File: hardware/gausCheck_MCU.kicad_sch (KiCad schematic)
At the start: 1 part, among them U3 ATSAML22N18A-AUT

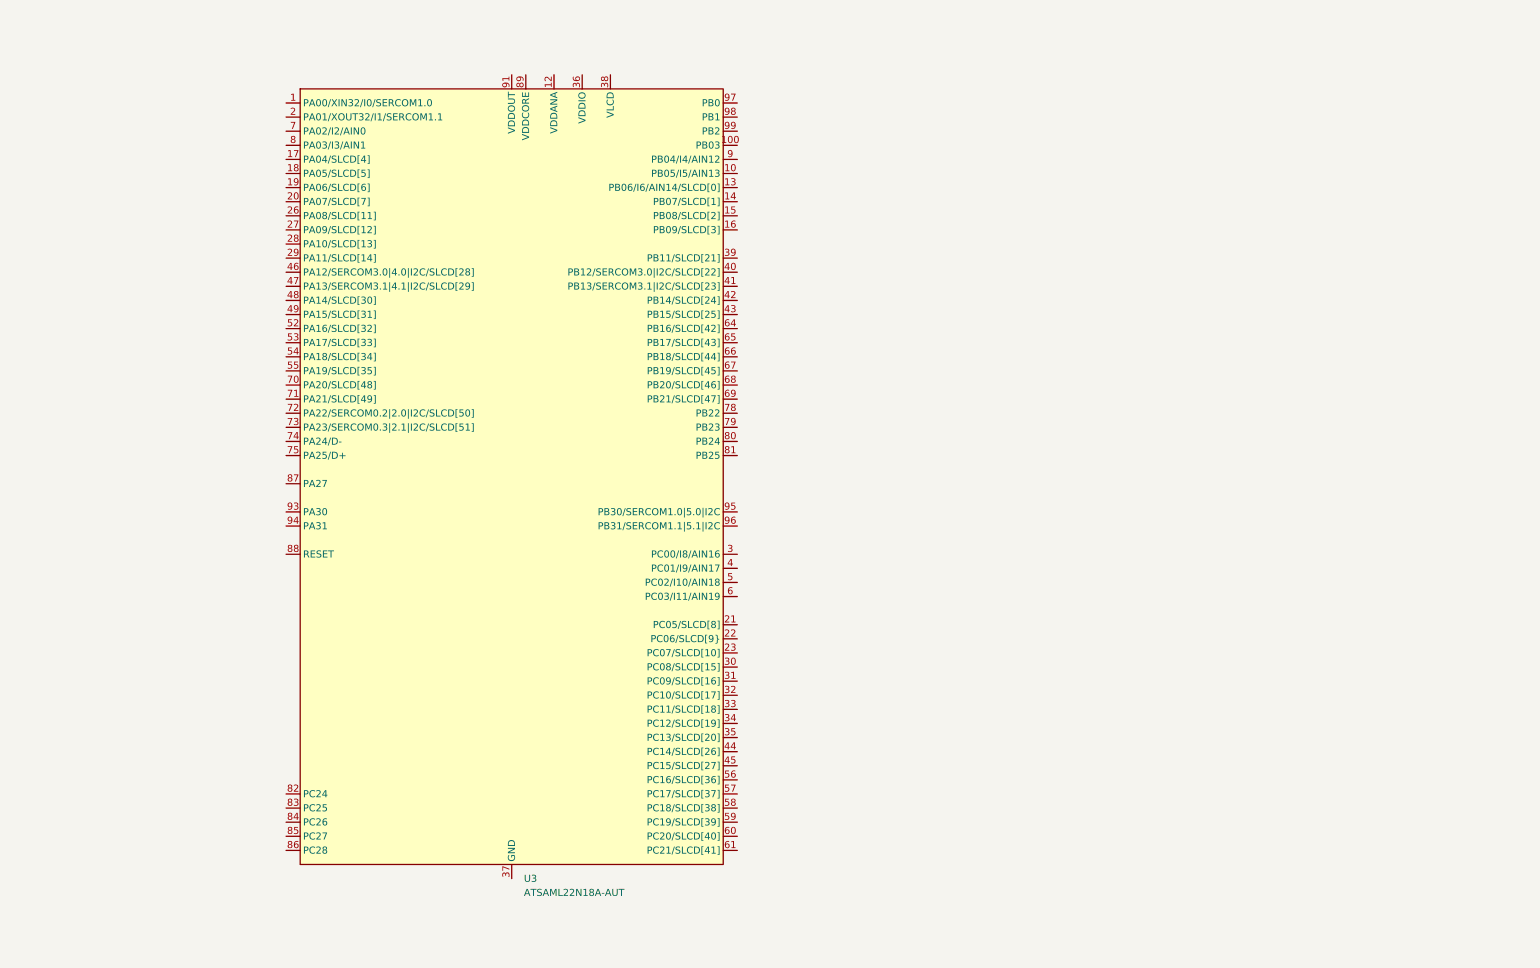
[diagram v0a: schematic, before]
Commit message: SCH - display lines
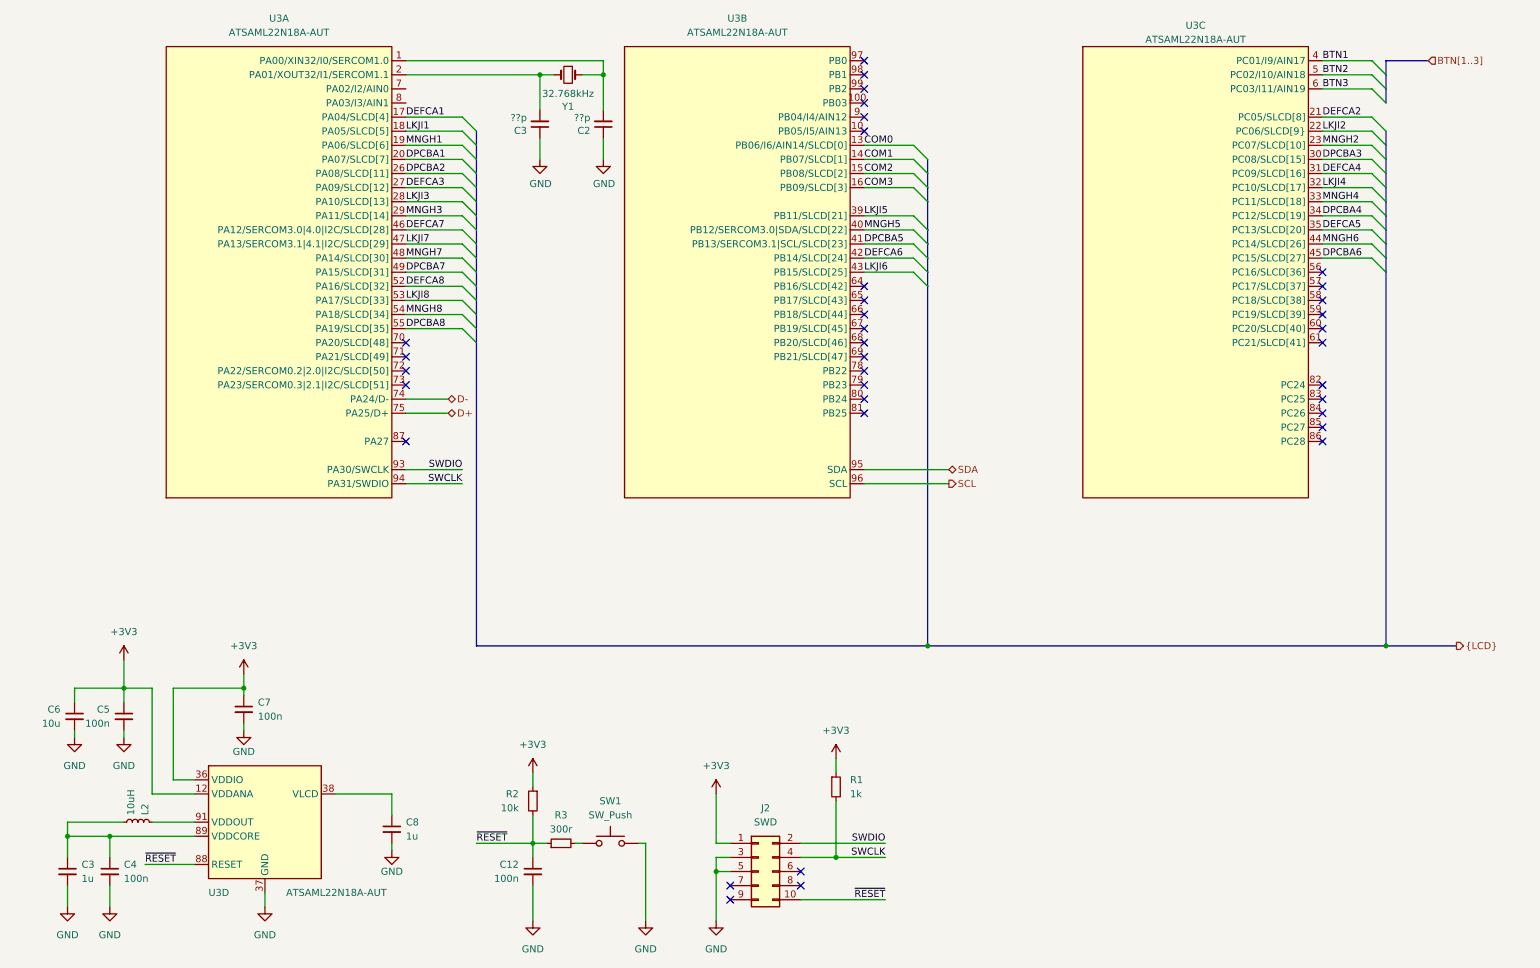
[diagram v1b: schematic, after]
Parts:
- removed U3: ATSAML22N18A-AUT, Package_QFP:TQFP-100_14x14mm_P0.5mm, symbol GaussCheckCustomSymbols:ATSAML22N18A-AUT
- added C12, C4, C5, C7: 100n, symbol Device:C_Small
- added C2, C3: ??p, Capacitor_SMD:C_0603_1608Metric, symbol MagnetoStage-rescue:C_Small-Device
- added C3, C8: 1u, symbol Device:C_Small
- added C6: 10u, symbol Device:C_Small
- added J2: SWD, symbol Connector_Generic:Conn_02x05_Odd_Even
- added L2: 10uH, symbol Device:L_Small
- added R1: 1k, symbol Device:R_Small
- added R2: 10k, symbol Device:R_Small
- added R3: 300r, symbol Device:R_Small
- added SW1: SW_Push, symbol Switch:SW_Push
- added U3: ATSAML22N18A-AUT, Package_QFP:TQFP-100_14x14mm_P0.5mm, symbol GaussCheckCustomSymbols:ATSAML22N18A-AUT (Multi)
- added Y1: 32.768kHz, Crystal:Crystal_SMD_3215-2Pin_3.2x1.5mm, symbol MagnetoStage-rescue:Crystal_32.7680kHz_12.5pF_SMD-Knochi_Crystals
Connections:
- new net: R3.2, SW1.1
- new net: C3.1, C4.1, L2.2, U3.89 (VDDCORE)
- new net: L2.1, U3.91 (VDDOUT)
- new net: C8.1, U3.38 (VLCD)
- new net: C2.2, U3.1 (PA00/XIN32/I0/SERCOM1.0), Y1.1
- new net: C3.2, U3.2 (PA01/XOUT32/I1/SERCOM1.1), Y1.4
- new net +3V3: C5.1, C6.1, C7.1, J2.1 (Pin_1), R1.1, R2.1, U3.12 (VDDANA), U3.25 (VDDANA), U3.36 (VDDIO), U3.51 (VDDIO), U3.63 (VDDIO), U3.77 (VDDIO), U3.92 (VDDIO)
- new net BTN1: U3.4 (PC01/I9/AIN17)
- new net BTN2: U3.5 (PC02/I10/AIN18)
- new net BTN3: U3.6 (PC03/I11/AIN19)
- new net COM0: U3.13 (PB06/I6/AIN14/SLCD[0])
- new net COM1: U3.14 (PB07/SLCD[1])
- new net COM2: U3.15 (PB08/SLCD[2])
- new net COM3: U3.16 (PB09/SLCD[3])
- new net D+: U3.75 (PA25/D+)
- new net D-: U3.74 (PA24/D-)
- new net DEFCA1: U3.17 (PA04/SLCD[4])
- new net DEFCA2: U3.21 (PC05/SLCD[8])
- new net DEFCA3: U3.27 (PA09/SLCD[12])
- new net DEFCA4: U3.31 (PC09/SLCD[16])
- new net DEFCA5: U3.35 (PC13/SLCD[20])
- new net DEFCA6: U3.42 (PB14/SLCD[24])
- new net DEFCA7: U3.46 (PA12/SERCOM3.0|4.0|I2C/SLCD[28])
- new net DEFCA8: U3.52 (PA16/SLCD[32])
- new net DPCBA1: U3.20 (PA07/SLCD[7])
- new net DPCBA2: U3.26 (PA08/SLCD[11])
- new net DPCBA3: U3.30 (PC08/SLCD[15])
- new net DPCBA4: U3.34 (PC12/SLCD[19])
- new net DPCBA5: U3.41 (PB13/SERCOM3.1|SCL/SLCD[23])
- new net DPCBA6: U3.45 (PC15/SLCD[27])
- new net DPCBA7: U3.49 (PA15/SLCD[31])
- new net DPCBA8: U3.55 (PA19/SLCD[35])
- new net GND: C12.2, C2.1, C3.1, C3.2, C4.2, C5.2, C6.2, C7.2, C8.2, J2.3 (Pin_3), J2.5 (Pin_5), SW1.2, U3.11 (GND), U3.24 (GND), U3.37 (GND), U3.50 (GND), U3.62 (GND), U3.76 (GND), U3.90 (GND)
- new net LKJI1: U3.18 (PA05/SLCD[5])
- new net LKJI2: U3.22 (PC06/SLCD[9})
- new net LKJI3: U3.28 (PA10/SLCD[13])
- new net LKJI4: U3.32 (PC10/SLCD[17])
- new net LKJI5: U3.39 (PB11/SLCD[21])
- new net LKJI6: U3.43 (PB15/SLCD[25])
- new net LKJI7: U3.47 (PA13/SERCOM3.1|4.1|I2C/SLCD[29])
- new net LKJI8: U3.53 (PA17/SLCD[33])
- new net MNGH1: U3.19 (PA06/SLCD[6])
- new net MNGH2: U3.23 (PC07/SLCD[10])
- new net MNGH3: U3.29 (PA11/SLCD[14])
- new net MNGH4: U3.33 (PC11/SLCD[18])
- new net MNGH5: U3.40 (PB12/SERCOM3.0|SDA/SLCD[22])
- new net MNGH6: U3.44 (PC14/SLCD[26])
- new net MNGH7: U3.48 (PA14/SLCD[30])
- new net MNGH8: U3.54 (PA18/SLCD[34])
- new net SCL: U3.96 (PB31/SERCOM1.1|5.1|SCL)
- new net SDA: U3.95 (PB30/SERCOM1.0|5.0|SDA)
- new net SWCLK: J2.4 (Pin_4), R1.2, U3.94 (PA31/SWDIO)
- new net SWDIO: J2.2 (Pin_2), U3.93 (PA30/SWCLK)
- new net ~{RESET}: C12.1, J2.10 (Pin_10), R2.2, R3.1, U3.88 (RESET)
- no-connect marks 0 -> 36

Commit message: more schematic work, added buttons and led lcd wiring done
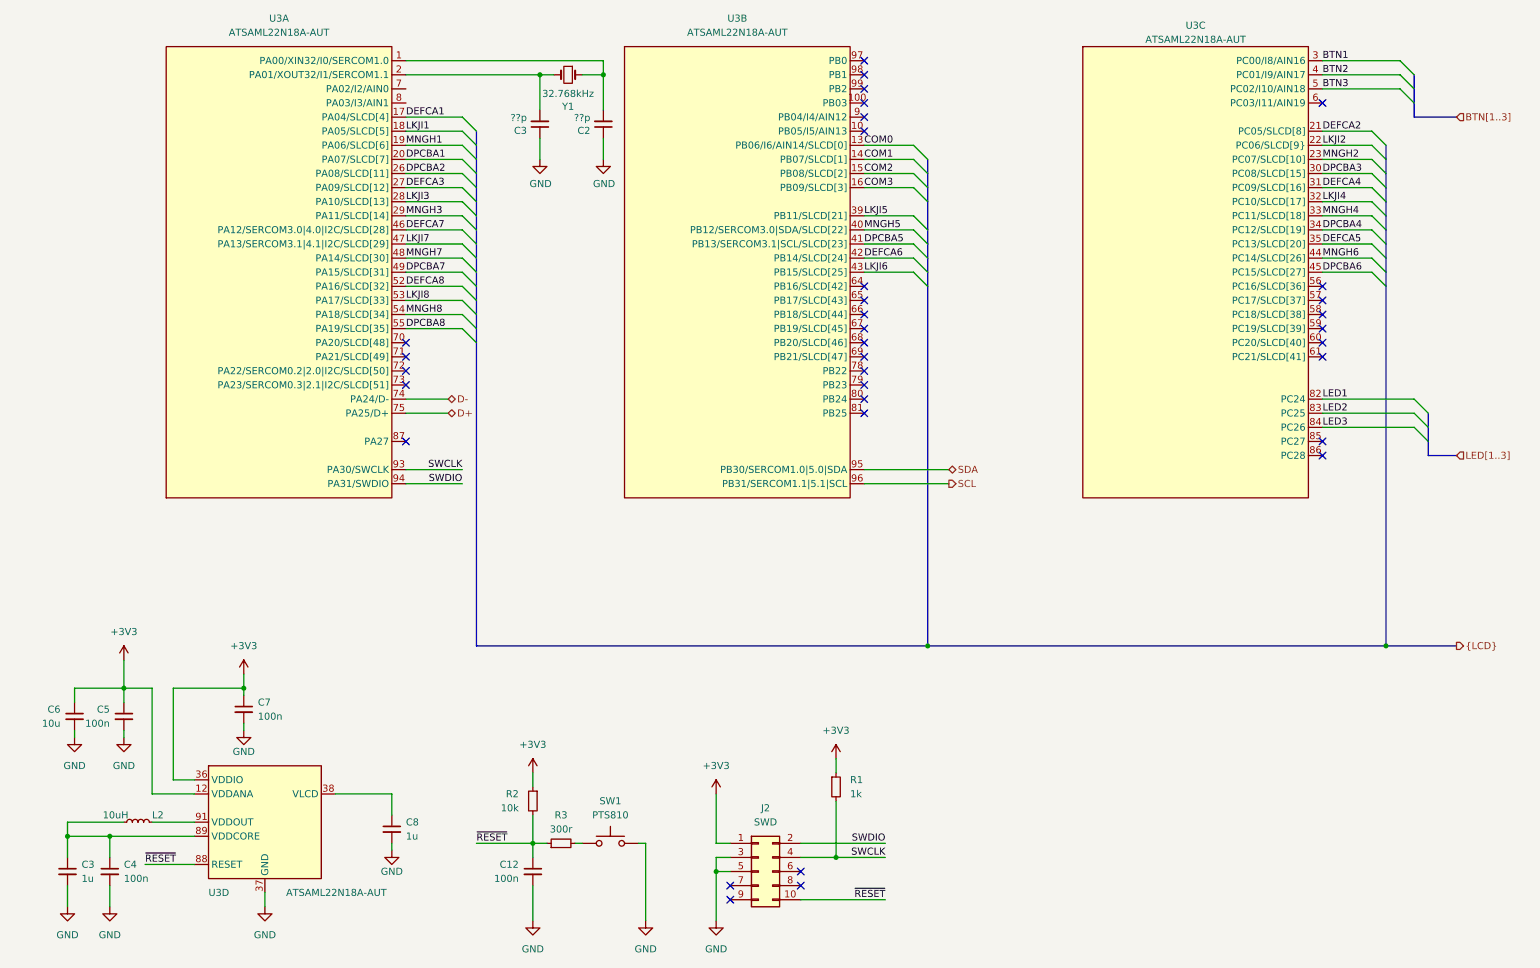
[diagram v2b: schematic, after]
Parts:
- C12, C3, C4, C5, C6, C7, C8: footprint (none) -> Capacitor_SMD:C_0603_1608Metric
- J2: footprint (none) -> Connector_PinHeader_1.27mm:PinHeader_2x05_P1.27mm_Vertical_SMD
- L2: footprint (none) -> Inductor_SMD:L_Taiyo-Yuden_MD-4040; MPN (none) -> LSXBD4040KKL100M
- R1, R2, R3: footprint (none) -> Resistor_SMD:R_0603_1608Metric
- SW1: value SW_Push -> PTS810; footprint (none) -> Button_Switch_SMD:SW_SPST_PTS810
- Y1: symbol MagnetoStage-rescue:Crystal_32.7680kHz_12.5pF_SMD-Knochi_Crystals -> Device:Crystal_Small
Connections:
- net BTN1: now also U3.3 (PC00/I8/AIN16); no longer U3.4 (PC01/I9/AIN17)
- net BTN2: now also U3.4 (PC01/I9/AIN17); no longer U3.5 (PC02/I10/AIN18)
- net BTN3: now also U3.5 (PC02/I10/AIN18); no longer U3.6 (PC03/I11/AIN19)
- net SWCLK: now also U3.93 (PA30/SWCLK); no longer U3.94 (PA31/SWDIO)
- net SWDIO: now also U3.94 (PA31/SWDIO); no longer U3.93 (PA30/SWCLK)
- net at C3.2, U3.2 (PA01/XOUT32/I1/SERCOM1.1): now also Y1.2; no longer Y1.4
- net LED1: now reaches U3.82 (PC24)
- net LED2: now reaches U3.83 (PC25)
- net LED3: now reaches U3.84 (PC26)
- no-connect marks 36 -> 34

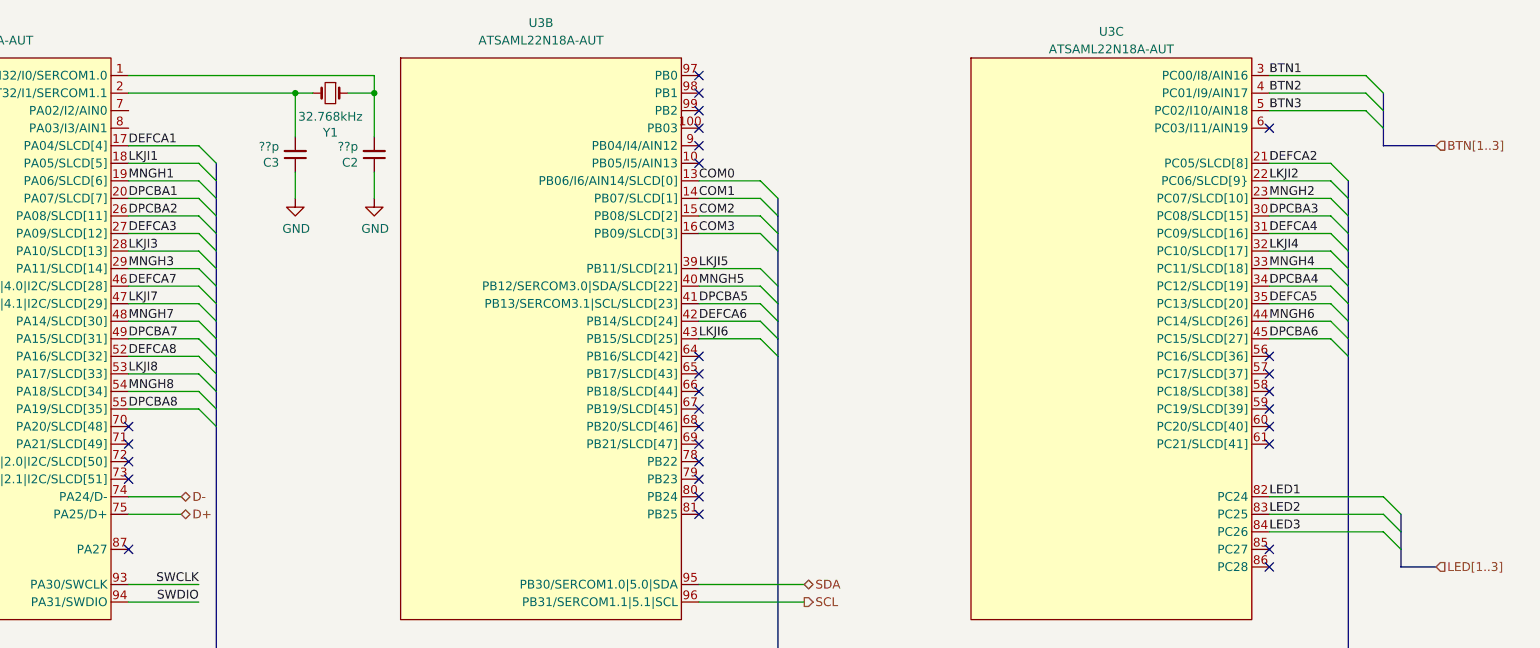
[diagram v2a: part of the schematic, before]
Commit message: change btn in sch, routing
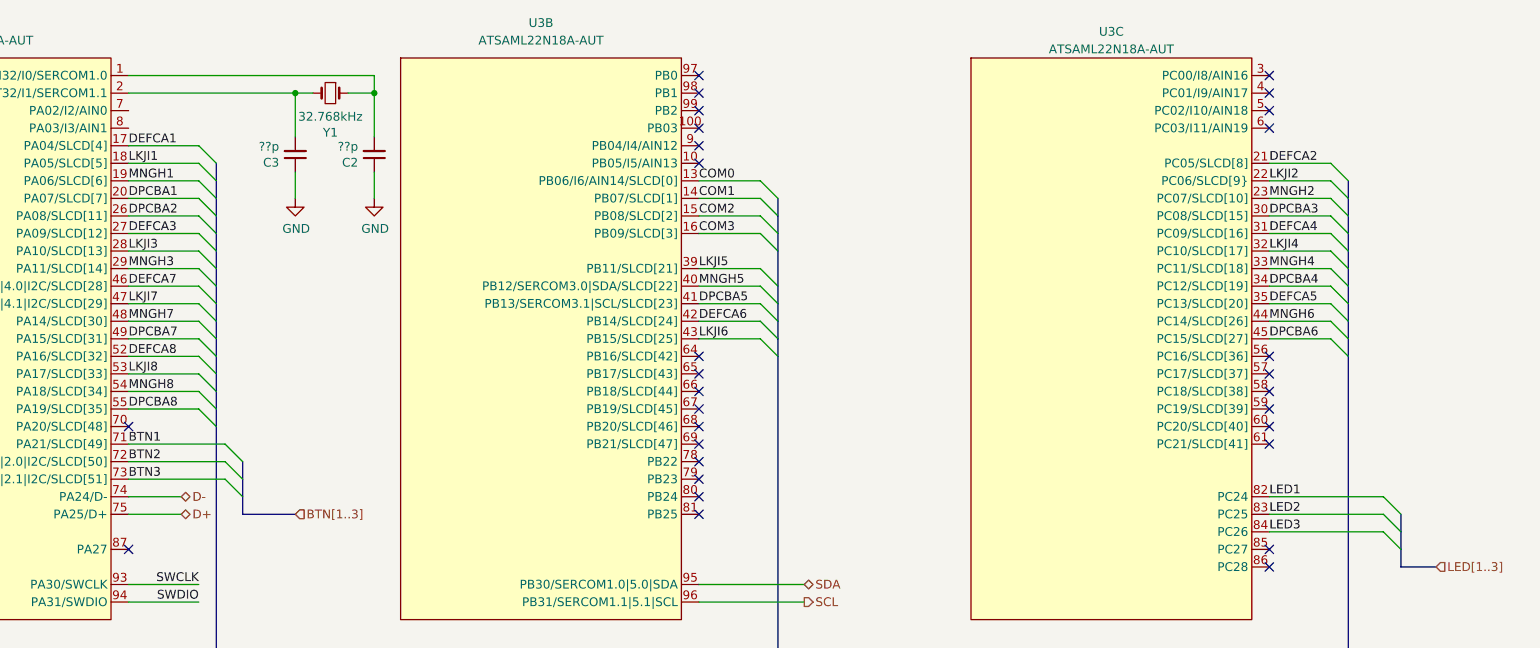
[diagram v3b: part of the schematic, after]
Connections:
- net BTN1: now also U3.71 (PA21/SLCD[49]); no longer U3.3 (PC00/I8/AIN16)
- net BTN2: now also U3.72 (PA22/SERCOM0.2|2.0|I2C/SLCD[50]); no longer U3.4 (PC01/I9/AIN17)
- net BTN3: now also U3.73 (PA23/SERCOM0.3|2.1|I2C/SLCD[51]); no longer U3.5 (PC02/I10/AIN18)

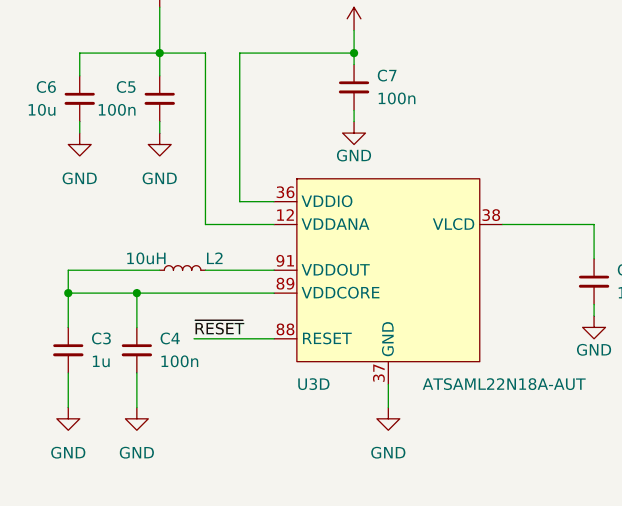
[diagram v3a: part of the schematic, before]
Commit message: Turned MCU by 45degress and rerouted
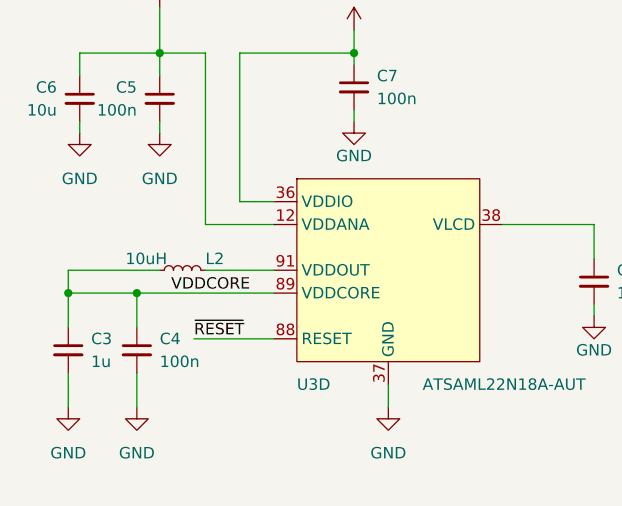
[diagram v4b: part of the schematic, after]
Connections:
- net VDDCORE: now reaches C3.1, C4.1, L2.2, U3.89 (VDDCORE)
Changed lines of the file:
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@@
+    (effects (font (size 1.27 1.27)) (justify left bottom))
+  )
+  (label "VDDCORE" (at 33.02 170.18 0) (fields_autoplaced)
     (effects (font (size 1.27 1.27)) (justify left bottom))
   )

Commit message: minor adjustments
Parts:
- L2: footprint Inductor_SMD:L_Taiyo-Yuden_MD-4040 -> Inductor_SMD:L_0805_2012Metric; DCR (none) -> 650 mOhms; ISat (none) -> 200mA; MPN LSXBD4040KKL100M -> MLZ2012M100HT000
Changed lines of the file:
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@@
       (effects (font (size 1.27 1.27)) (justify left))
     )
-    (property "Footprint" "Inductor_SMD:L_Taiyo-Yuden_MD-4040" (at 34.29 167.64 0)
+    (property "Footprint" "Inductor_SMD:L_0805_2012Metric" (at 34.29 167.64 0)
       (effects (font (size 1.27 1.27)) hide)
     )
-    (property "Datasheet" "~" (at 34.29 167.64 0)
+    (property "Datasheet" "https://product.tdk.com/system/files/dam/doc/product/inductor/inductor/smd/catalog/inductor_commercial_decoupling_mlz2012_en.pdf" (at 34.29 167.64 0)
       (effects (font (size 1.27 1.27)) hide)
     )
-    (property "MPN" "LSXBD4040KKL100M" (at 34.29 167.64 90)
+    (property "MPN" "MLZ2012M100HT000" (at 34.29 167.64 90)
       (effects (font (size 1.27 1.27)) hide)
     )
+    (property "ISat" "200mA" (at 38.1 163.83 90)
+      (effects (font (size 1.27 1.27)))
+    )
+    (property "DCR" "650 mOhms" (at 27.94 163.83 90)
+      (effects (font (size 1.27 1.27)))
+    )
     (pin "1")
